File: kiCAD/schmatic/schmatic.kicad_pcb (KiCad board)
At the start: 2 copper layers, 33.5 x 34.5 mm, 43 parts, among them J2 Conn_02x03_Counter_Clockwise, J3 Connector, USB-TYPE-C-16P, U1 AMS1117, U2 MS561101BA03-50, U4 MPU-9250, U6 STM32F103C8T6, X1 X322516MLB4SI, X2 Q13FC1350000400

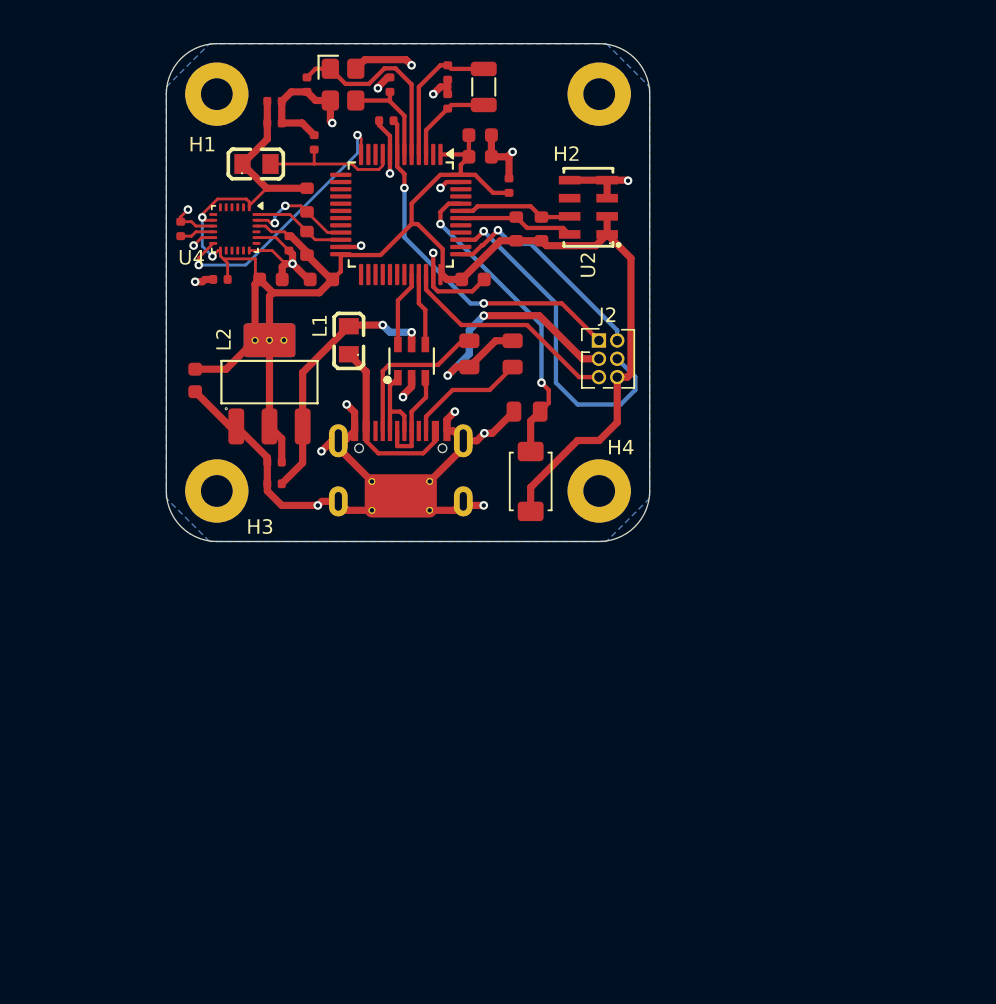
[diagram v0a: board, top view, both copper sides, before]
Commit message: feat: modified PCB flight computer for extended features
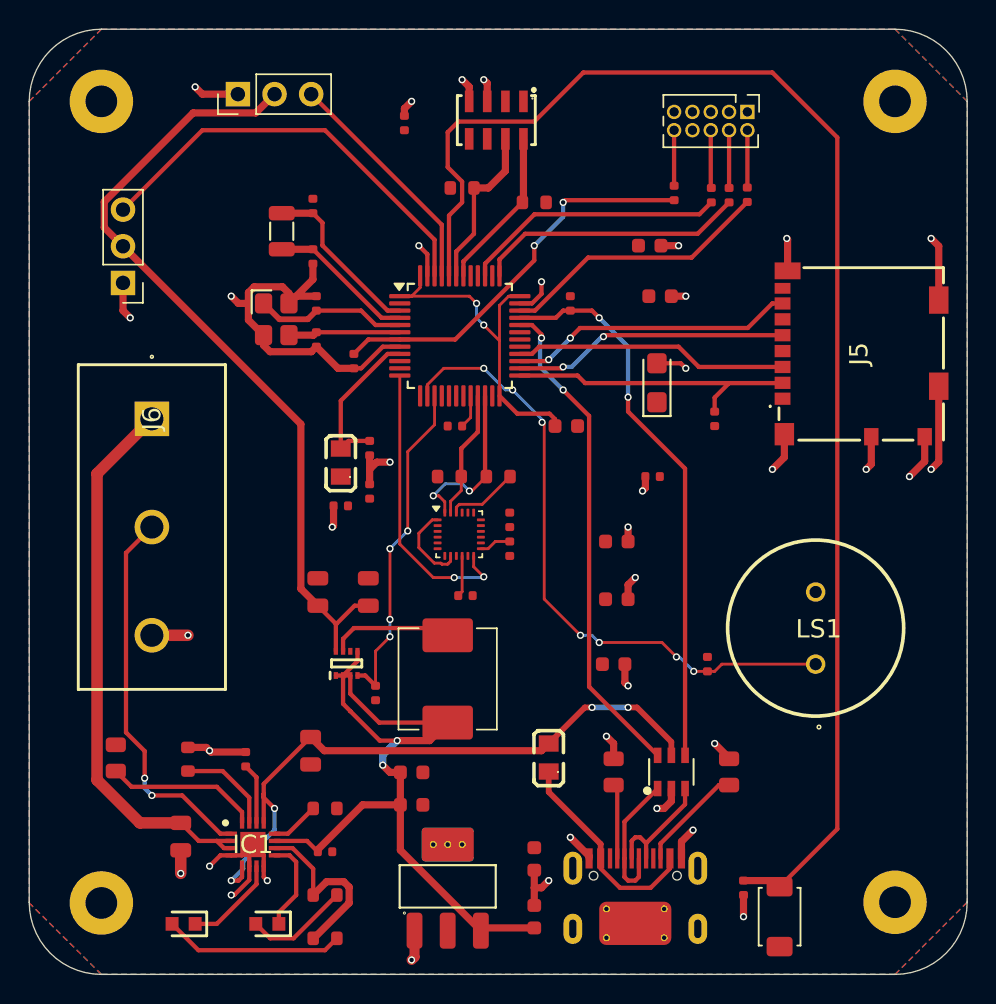
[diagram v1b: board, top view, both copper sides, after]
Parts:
- added C19: 10uF, PCM_JLCPCB:C_CASE-A-3216-18(mm), F.Cu at (160.0, 105.5)
- added C20: 10uF, PCM_JLCPCB:C_0805, F.Cu at (136.0, 131.0)
- added C21: 10uF, PCM_JLCPCB:C_0805, F.Cu at (127.0, 136.9)
- added C25: 10pF, PCM_JLCPCB:C_0402, F.Cu at (137.0, 138.0)
- added C26: 10uF, PCM_JLCPCB:C_0603, F.Cu at (143.0, 132.5)
- added C27: 10uF, PCM_JLCPCB:C_0603, F.Cu at (143.0, 134.8)
- added C28: 22uF, PCM_JLCPCB:C_0805, F.Cu at (136.5, 120.0)
- added C29: 22uF, PCM_JLCPCB:C_0805, F.Cu at (140.0, 120.0)
- added C6: 10uF, PCM_JLCPCB:C_0603, F.Cu at (151.5, 138.5)
- added IC1: BQ24074RGTT, Flight_computer:QFN50P300X300X100-17N-D, F.Cu at (132.0, 137.5)
- added J1: Conn_01x03_Socket, Connector_PinHeader_2.54mm:PinHeader_1x03_P2.54mm_Vertical, F.Cu at (131.0, 85.5)
- added J4: Conn_01x03_Socket, Connector_PinHeader_2.54mm:PinHeader_1x03_P2.54mm_Vertical, F.Cu at (123.0, 98.6)
- added J5: 104031-0811, Flight_computer:1040310811, F.Cu at (174.0, 103.5)
- added J6: TB004-750-03GR, Flight_computer:TB004-750-03GR, F.Cu at (125.0, 108.0)
- added L3: L, Inductor_SMD:L_APV_APH0620, F.Cu at (145.5, 126.0)
- added LED1: LTST-C190KGKT, Flight_computer:LEDC1608X80N, F.Cu at (127.2, 143.0)
- added LED2: LTST-C190KGKT, Flight_computer:LEDC1608X80N, F.Cu at (133.0, 143.0)
- added LS1: PS1240P02CT3, Flight_computer:PS1240P02BT, F.Cu at (171.0, 122.5)
- added PS1: TPS61033DRLR, Flight_computer:SOTFL50P160X60-8N, F.Cu at (138.5, 125.0)
- added R10: 10kΩ, PCM_JLCPCB:R_0402, F.Cu at (164.0, 108.0)
- added R11: 1.5kΩ, PCM_JLCPCB:R_0402, F.Cu at (163.5, 125.0)
- added R12: 22Ω, PCM_JLCPCB:R_0402, F.Cu at (166.3, 92.5)
- added R13: 22Ω, PCM_JLCPCB:R_0402, F.Cu at (165.0, 92.5)
- added R14: 22Ω, PCM_JLCPCB:R_0402, F.Cu at (163.8, 92.5)
- added R15: 22Ω, PCM_JLCPCB:R_0402, F.Cu at (161.2, 92.3)
- added R16: 1.1kΩ, PCM_JLCPCB:R_0603, F.Cu at (137.0, 135.0)
- added R17: 1.1kΩ, PCM_JLCPCB:R_0603, F.Cu at (127.5, 131.6)
- added R18: 750Ω, PCM_JLCPCB:R_0805, F.Cu at (122.5, 131.5)
- added R19: 49.9kΩ, PCM_JLCPCB:R_0402, F.Cu at (131.5, 131.6)
- added R20: 1.1kΩ, PCM_JLCPCB:R_0603, F.Cu at (137.0, 141.0)
- added R21: 1.1kΩ, PCM_JLCPCB:R_0603, F.Cu at (137.0, 144.0)
- added R22: 10kΩ, PCM_JLCPCB:R_0402, F.Cu at (140.5, 127.0)
- added R8: 1.5kΩ, PCM_JLCPCB:R_0402, F.Cu at (154.0, 100.0)
- added R9: 10kΩ, PCM_JLCPCB:R_0402, F.Cu at (146.0, 108.5)
- C15: value 100nF -> 10uF; footprint PCM_JLCPCB:C_0402 -> PCM_JLCPCB:C_0603
- J2: value Conn_02x03_Counter_Clockwise -> Conn_02x05_Odd_Even; footprint Connector_PinHeader_1.27mm:PinHeader_2x03_P1.27mm_Vertical -> Connector_PinHeader_1.27mm:PinHeader_2x05_P1.27mm_Vertical
- R6: value 5.1kΩ -> 10kΩ; footprint PCM_JLCPCB:R_0805 -> PCM_JLCPCB:R_0402
- moved H2 59.6 mm to (176.5, 141.5)
- moved H1 56.6 mm to (121.5, 141.6)
- moved U1 37.1 mm to (145.5, 140.5)
- moved R6 36.2 mm to (166.0, 140.5), turned to 90 degrees
- moved C9 35.0 mm to (157.0, 125.0), turned to 0 degrees
- moved C15 35.0 mm to (151.5, 142.5), turned to 90 degrees
- moved S1 34.7 mm to (168.5, 142.5)
- moved H4 33.9 mm to (176.5, 86.0)
- moved J3 33.8 mm to (158.5, 141.0)
- moved D1 33.7 mm to (161.0, 132.5)
- moved R4 32.6 mm to (165.0, 132.5)
- moved C24 32.2 mm to (146.7, 120.2), turned to 0 degrees
- moved L1 32.1 mm to (152.5, 131.5)
- moved R5 30.6 mm to (157.0, 132.5), turned to 90 degrees
- moved H3 28.2 mm to (121.5, 86.0)
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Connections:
- C15 pad 1: +5V -> VDD
- J2 pad 1: /NRST -> +3.3VP
- J2 pad 2: /SWCLK -> Net-(J2-Pin_2)
- J2 pad 4: /SWO -> Net-(J2-Pin_4)
- J2 pad 5: /SWDIO -> GND
- J2 pad 6: +3.3VP -> Net-(J2-Pin_6)
- U1 pad 3: +5V -> VDD
- U2 pad 5: GND -> unconnected-(U2-CSB-Pad5)
- U6 pad 14: unconnected-(U6-PA4-Pad14) -> /buzzer
- U6 pad 15: unconnected-(U6-PA5-Pad15) -> /PG
- U6 pad 20: unconnected-(U6-PB2-Pad20) -> /Boot1
- U6 pad 25: unconnected-(U6-PB12-Pad25) -> /CD/DAT3
- U6 pad 26: unconnected-(U6-PB13-Pad26) -> /SPI2_SCK
- U6 pad 27: unconnected-(U6-PB14-Pad27) -> /SPI2_MISO
- U6 pad 28: unconnected-(U6-PB15-Pad28) -> /SPI2_MOSI
- U6 pad 45: unconnected-(U6-PB8-Pad45) -> /S0
- U6 pad 46: unconnected-(U6-PB9-Pad46) -> /S1
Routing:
- net +3.3VP: track 126.7 -> 37.2 mm
- net /Boot0: track 21.9 -> 97.6 mm, vias 2 -> 0
- net VDD: track 0.00 -> 66.5 mm, vias 0 -> 2
- net +5VD: track 0.00 -> 55.5 mm
- net /buzzer: track 0.00 -> 44.2 mm, vias 0 -> 7
- net /BAT+: track 0.00 -> 38.9 mm
- net /D+: track 5.04 -> 38.7 mm, vias 0 -> 2
- net /S1: track 0.00 -> 29.5 mm
- net /D-: track 5.24 -> 34.4 mm, vias 0 -> 2
- net /TS: track 0.00 -> 26.7 mm, vias 0 -> 2
- net +5V: track 18.4 -> 45.0 mm, vias 2 -> 4
- net /PG: track 0.00 -> 23.3 mm, vias 0 -> 4
- net /CD/DAT3: track 0.00 -> 20.8 mm
- net /SPI2_MISO: track 0.00 -> 19.9 mm, vias 0 -> 2
- net /SPI2_SCK: track 0.00 -> 19.2 mm, vias 0 -> 2
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- added copper zone on F.Cu, net +3.3VP
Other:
- board size 33.5 x 34.5 mm -> 65 x 65.5 mm
